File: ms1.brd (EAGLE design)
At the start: 160 x 100 mm, 146 parts, among them IC1 MAX3232EUE, IC2 MAX3380EEUP, J1 POWERPOLE_POWER25A, J10 Radio, J11 A3, J12 A4, J13 A5, J14 A6, J15 A7, J16 D1, J17 D2, J18 D3, J19 D4, J2 ON, J20 D5, J21 D6, J22 D7, J3 LED-EN, J4 RS232, J5 RS485, J6 A1, J7 I2C, J8 A2, J9 TTL_SERIAL, Q1 DMG6602SVT, Q2 DMG6602SVT, Q3 DMG6602SVT, Q4 DMG6602SVT, U1 LT1934ES6TRMPBF, U2 LT1934ES6TRMPBF, U3 DS3231SN, U4 ISL3179EIBZ, X1 KUSBVX-BS1N

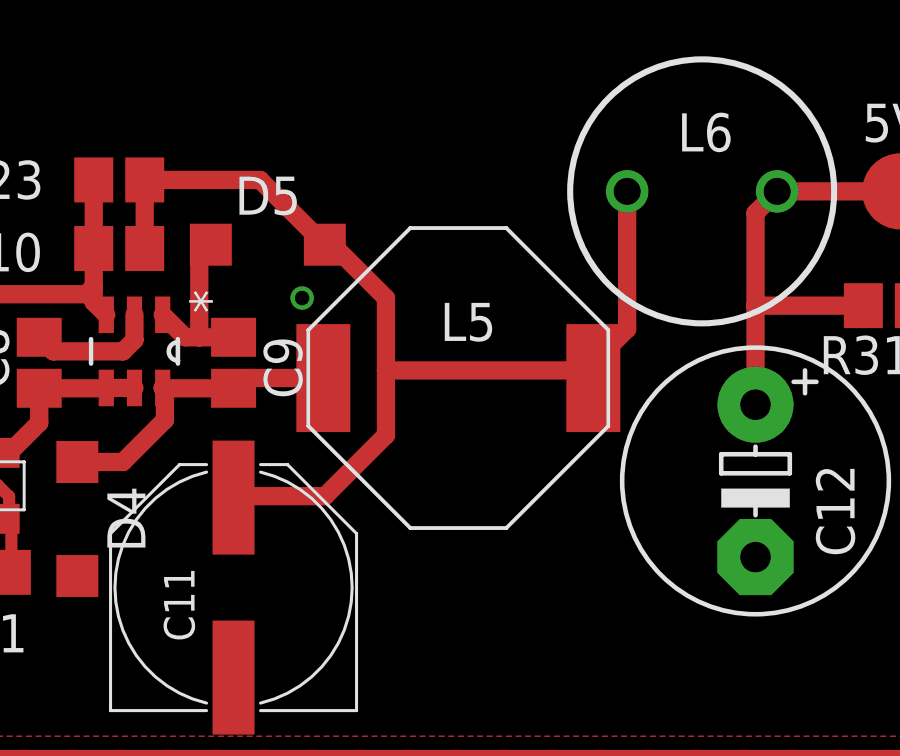
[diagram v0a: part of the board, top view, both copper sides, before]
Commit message: now uses dr127 for 5w inductor
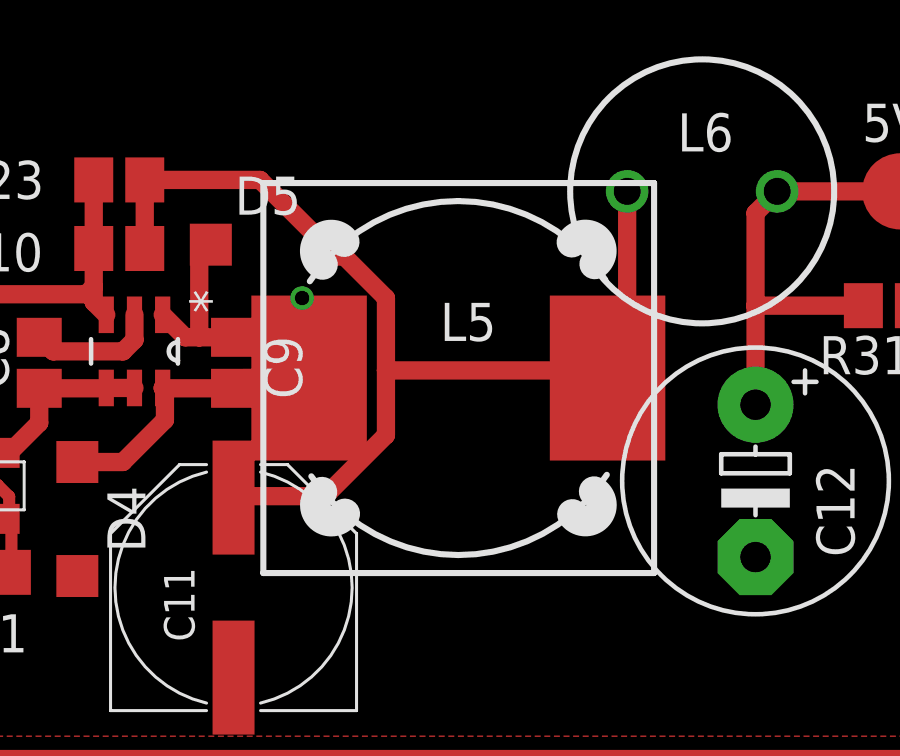
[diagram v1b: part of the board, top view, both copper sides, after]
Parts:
- L5: device farnell-parts:1048 -> inductors:DR127
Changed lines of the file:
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@@
 <attribute name="NAME" x="121.285" y="92.202" size="1.27" layer="25" rot="R180"/>
 </element>
-<element name="L5" library="farnell-parts" package="1048" value="68uH" x="135.128" y="87.376" smashed="yes">
+<element name="L5" library="inductors" package="DR127" value="68uH" x="135.128" y="87.376" smashed="yes">
 <attribute name="NAME" x="134.522" y="88.612" size="1.27" layer="25" ratio="10"/>
 </element>
@@
 <wire x1="125.2846" y1="87.034" x2="127.635" y2="87.034" width="0.6096" layer="1"/>
 <wire x1="127.635" y1="87.034" x2="127.977" y2="87.376" width="0.6096" layer="1"/>
-<wire x1="127.977" y1="87.376" x2="130.628" y2="87.376" width="0.6096" layer="1"/>
+<wire x1="127.977" y1="87.376" x2="130.153" y2="87.376" width="0.6096" layer="1"/>
 <wire x1="125.2728" y1="87.0458" x2="125.349" y2="86.9696" width="0.6096" layer="1"/>
 <wire x1="125.349" y1="86.9696" x2="125.349" y2="85.979" width="0.6096" layer="1"/>
@@
 <wire x1="132.715" y1="90.043" x2="130.937" y2="91.821" width="0.6096" layer="1"/>
 <wire x1="130.937" y1="91.821" x2="130.678" y2="91.821" width="0.6096" layer="1"/>
-<wire x1="139.628" y1="87.376" x2="139.374" y2="87.63" width="0.6096" layer="1"/>
+<wire x1="140.103" y1="87.376" x2="139.374" y2="87.63" width="0.6096" layer="1"/>
 <wire x1="139.374" y1="87.63" x2="132.715" y2="87.63" width="0.6096" layer="1"/>
 <wire x1="139.374" y1="87.63" x2="140.756" y2="89.012" width="0.6096" layer="1"/>

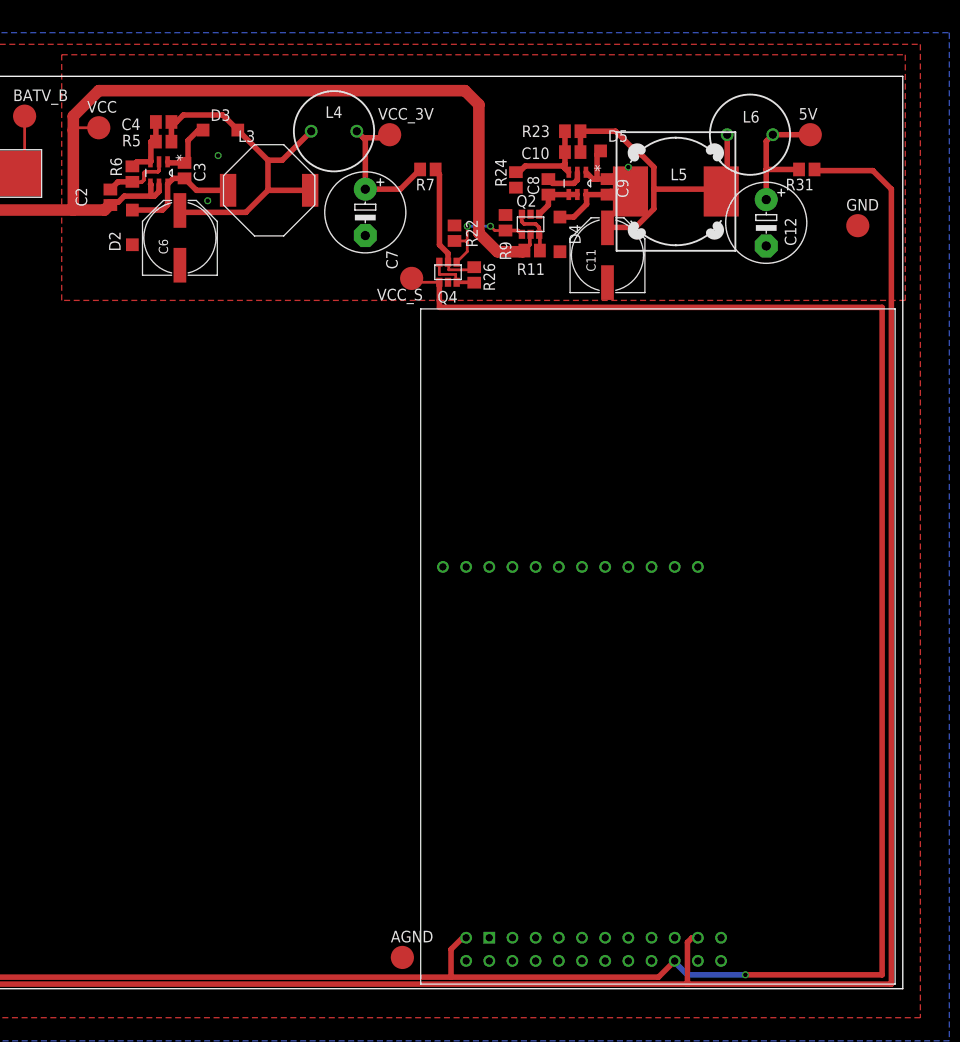
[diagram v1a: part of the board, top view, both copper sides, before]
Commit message: more smoothing to 5v rail
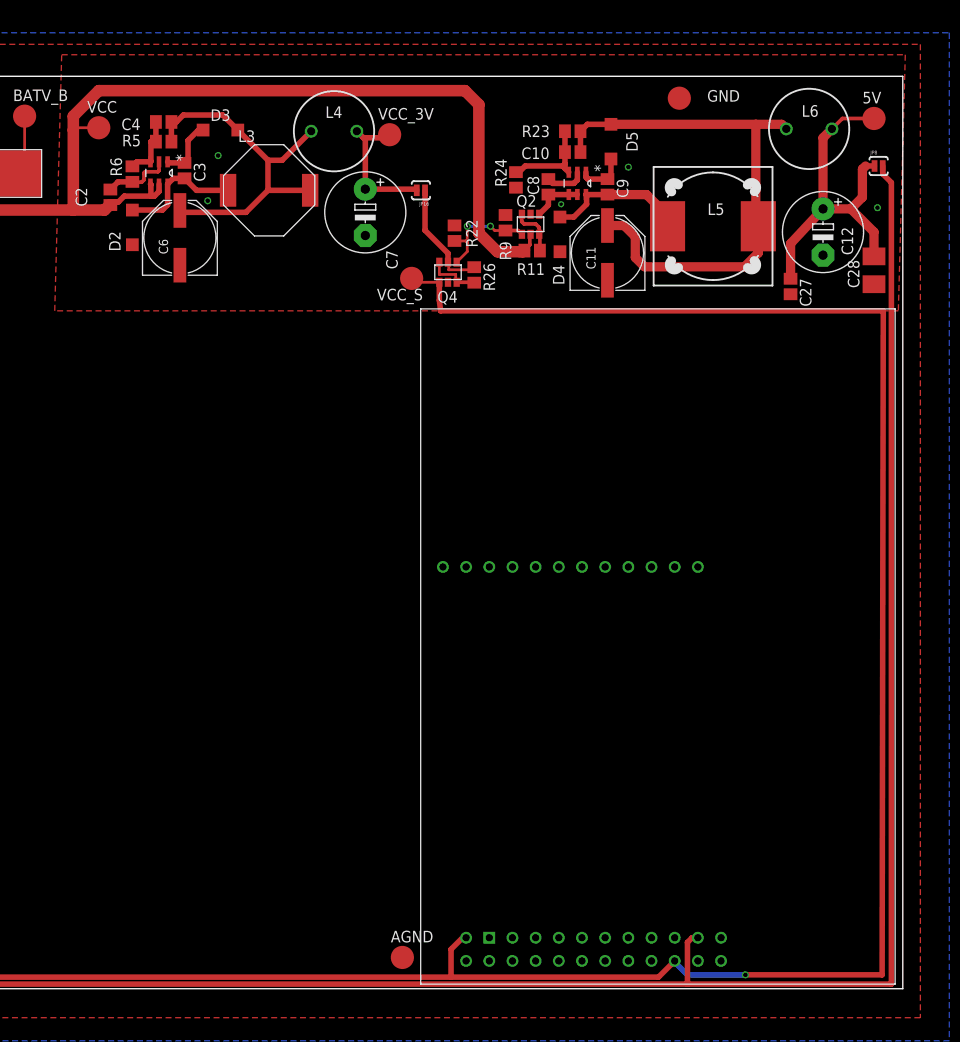
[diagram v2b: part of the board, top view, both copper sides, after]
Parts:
- removed R31, R7: TEST, resistor:R0805
- added C27: (no value), resistor:C0805
- added C28: (no value), resistor:B/3528-21R
- added JP16, JP8: (no value), SparkFun-Passives:SJ_2S-NO
- moved GND 24.0 mm to (135.5, 97.6)
- moved 5V 7.21 mm to (156.8, 95.4)
- moved L6 6.51 mm to (149.7, 94.2)
- moved C12 6.31 mm to (151.3, 82.9)
- moved L5 5.57 mm to (139.2, 83.6)
- moved D5 1.27 mm to (128.0, 92.8), turned to 90 degrees
- moved C11 0.25 mm to (127.6, 80.6)
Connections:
- net GND: now also C27.2, C28.-
- net N$13: now also JP16.2; no longer R7.2
- net N$14: now also C27.1, C28.+, JP8.1; no longer R31.2
- net SENSE_5V: now also JP8.2; no longer R31.1
- net VCC_3V3: now also JP16.1; no longer R7.1
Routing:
- net N$14: track 15.1 -> 39.0 mm
- net N$6: track 36.4 -> 60.1 mm
- net SENSE_5V: track 275.8 -> 269.4 mm
- net N$3: track 9.63 -> 15.7 mm
- net VCC_3V3: track 52.3 -> 50.6 mm
- net N$13: track 16.7 -> 15.5 mm
- net N$4: track 5.92 -> 5.35 mm
- net GND: vias 7 -> 9

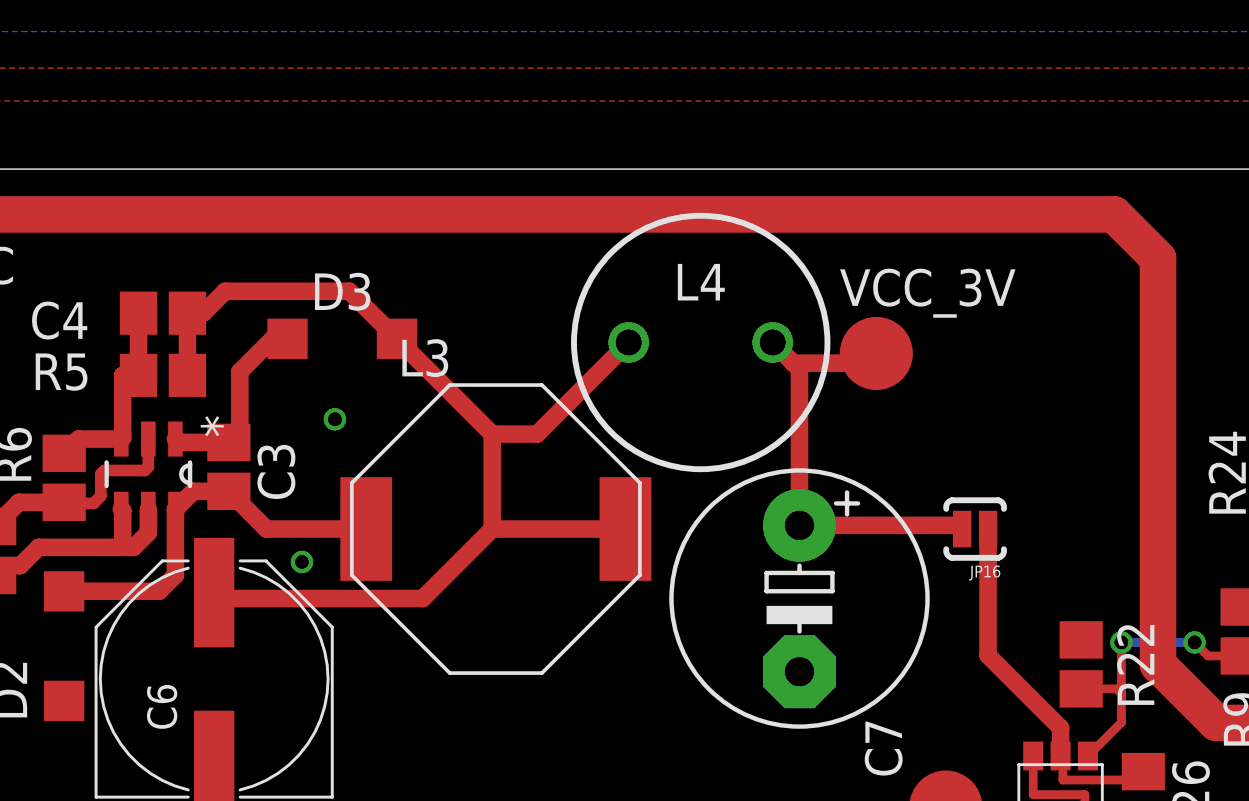
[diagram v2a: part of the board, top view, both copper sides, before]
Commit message: more smoothing on 3v3 output
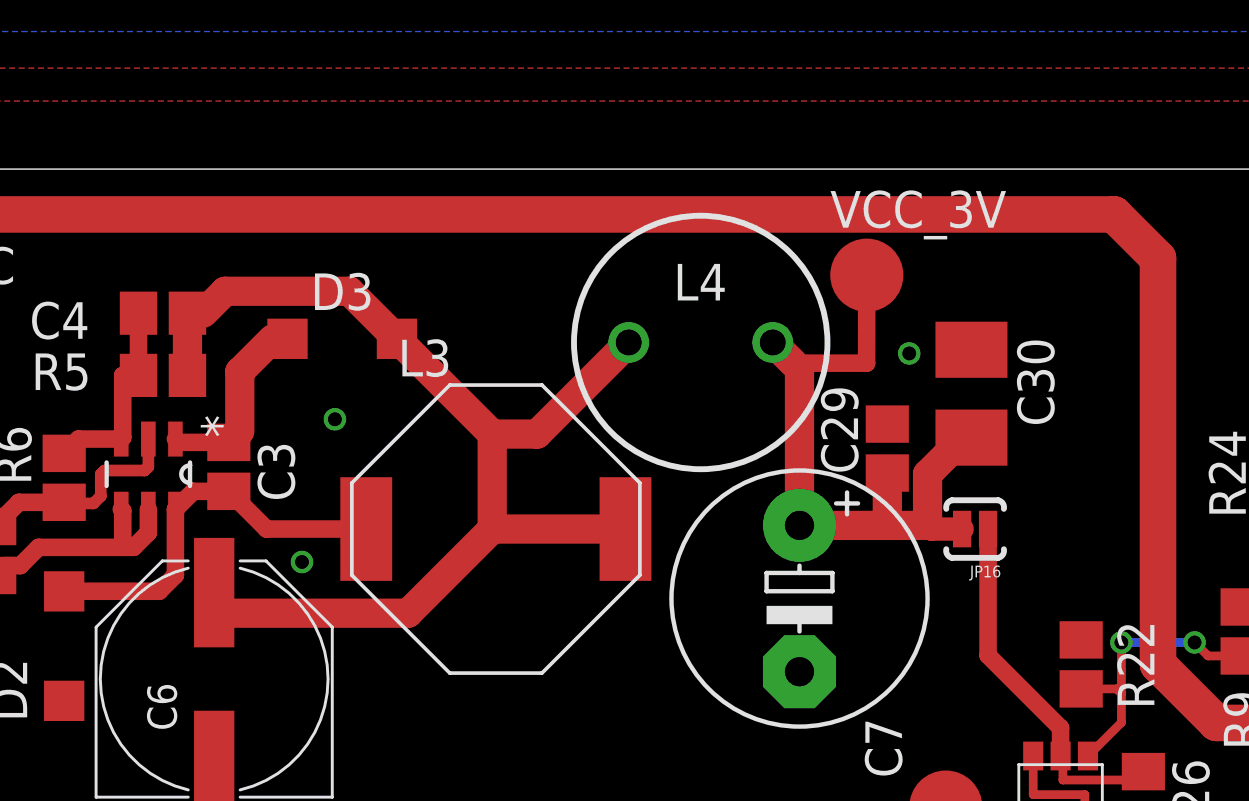
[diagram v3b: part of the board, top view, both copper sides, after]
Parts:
- added C29: (no value), resistor:C0805
- added C30: (no value), resistor:B/3528-21R
- moved VCC_3V 2.74 mm to (103.4, 96.3)
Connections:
- net GND: now also C29.2, C30.-
- net N$13: now also C29.1, C30.+
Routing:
- net N$13: track 15.5 -> 23.7 mm
- net N$107: track 39.8 -> 40.7 mm
- net GND: vias 9 -> 10
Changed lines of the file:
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@@
 <attribute name="NAME" x="84.117" y="95.107" size="1.27" layer="25"/>
 </element>
-<element name="VCC_3V" library="testpad" package="B2,54" value="TPB2,54" x="103.759" y="93.599">
-<attribute name="TP_SIGNAL_NAME" value="" x="210.439" y="-70.231" size="1.778" layer="27" display="off"/>
+<element name="VCC_3V" library="testpad" package="B2,54" value="TPB2,54" x="103.4288" y="96.3168">
+<attribute name="TP_SIGNAL_NAME" value="" x="210.1088" y="-67.5132" size="1.778" layer="27" display="off"/>
 </element>
 <element name="J2" library="farnell-parts" package="2-MOLEX" value="ON" x="5.715" y="96.2025" smashed="yes" rot="R270">
@@
 <element name="JP8" library="SparkFun-Passives" package="SJ_2S-NO" value="" x="157.353" y="90.17"/>
 <element name="JP16" library="SparkFun-Passives" package="SJ_2S-NO" value="" x="107.188" y="87.503" rot="R180"/>
+<element name="C29" library="resistor" package="C0805" value="" x="104.14" y="90.297" rot="R90"/>
+<element name="C30" library="resistor" package="B/3528-21R" value="" x="107.061" y="92.202" rot="R270"/>
 </elements>
 <signals>
@@
 <via x="122.555" y="85.979" extent="1-16" drill="0.381" shape="square"/>
 <via x="157.226" y="85.598" extent="1-16" drill="0.4826" shape="square"/>
+<contactref element="C30" pad="-"/>
+<contactref element="C29" pad="2"/>
+<via x="104.902" y="93.599" extent="1-16" drill="0.4826" shape="square"/>
 <wire x1="93.726" y1="136.017" x2="90.297" y2="143.549" width="0" layer="19" extent="16-16"/>
 <wire x1="93.726" y1="134.747" x2="93.726" y2="136.017" width="0" layer="19" extent="16-16"/>
@@
 <wire x1="84.328" y1="133.477" x2="84.328" y2="134.747" width="0" layer="19" extent="16-16"/>
 <wire x1="84.328" y1="132.207" x2="84.328" y2="133.477" width="0" layer="19" extent="16-16"/>
-<wire x1="84.963" y1="91.313" x2="93.726" y2="130.937" width="0" layer="19" extent="16-16"/>
+<wire x1="104.902" y1="93.599" x2="93.726" y2="130.937" width="0" layer="19" extent="16-16"/>
 <wire x1="-85.979" y1="97.663" x2="2.794" y2="64.516" width="0" layer="19" extent="1-1"/>
 <wire x1="-93.599" y1="97.663" x2="-85.979" y2="97.663" width="0" layer="19" extent="1-1"/>
@@
 <wire x1="79.541" y1="90.512" x2="81.28" y2="90.512" width="0.6096" layer="1"/>
 <wire x1="81.28" y1="90.512" x2="81.661" y2="90.893" width="0.6096" layer="1"/>
-<wire x1="81.661" y1="90.893" x2="81.661" y2="92.964" width="0.6096" layer="1"/>
-<wire x1="81.661" y1="92.964" x2="82.804" y2="94.107" width="0.6096" layer="1"/>
+<wire x1="81.661" y1="90.893" x2="81.661" y2="92.964" width="1.016" layer="1"/>
+<wire x1="81.661" y1="92.964" x2="82.804" y2="94.107" width="1.016" layer="1"/>
 <wire x1="82.804" y1="94.107" x2="83.317" y2="94.107" width="0.6096" layer="1"/>
 </signal>
@@
 <contactref element="C4" pad="1"/>
 <contactref element="L4" pad="1"/>
-<wire x1="79.844" y1="94.996" x2="79.844" y2="92.837" width="0.6096" layer="1"/>
-<wire x1="87.117" y1="94.107" x2="85.466" y2="95.758" width="0.6096" layer="1"/>
-<wire x1="85.466" y1="95.758" x2="81.153" y2="95.758" width="0.6096" layer="1"/>
-<wire x1="81.153" y1="95.758" x2="80.391" y2="94.996" width="0.6096" layer="1"/>
+<wire x1="79.844" y1="94.996" x2="79.844" y2="92.837" width="1.016" layer="1"/>
+<wire x1="87.117" y1="94.107" x2="85.466" y2="95.758" width="1.016" layer="1"/>
+<wire x1="85.466" y1="95.758" x2="81.153" y2="95.758" width="1.016" layer="1"/>
+<wire x1="81.153" y1="95.758" x2="80.391" y2="94.996" width="1.016" layer="1"/>
 <wire x1="80.391" y1="94.996" x2="79.844" y2="94.996" width="0.6096" layer="1"/>
-<wire x1="80.772" y1="85.296" x2="80.978" y2="85.09" width="0.6096" layer="1"/>
-<wire x1="80.978" y1="85.09" x2="88.011" y2="85.09" width="0.6096" layer="1"/>
-<wire x1="88.011" y1="85.09" x2="90.424" y2="87.503" width="0.6096" layer="1"/>
-<wire x1="90.424" y1="87.503" x2="95.051" y2="87.503" width="0.6096" layer="1"/>
-<wire x1="87.117" y1="94.107" x2="90.424" y2="90.8" width="0.6096" layer="1"/>
-<wire x1="90.424" y1="90.8" x2="90.424" y2="87.503" width="0.6096" layer="1"/>
-<wire x1="95.163" y1="93.98" x2="91.983" y2="90.8" width="0.6096" layer="1"/>
-<wire x1="91.983" y1="90.8" x2="90.424" y2="90.8" width="0.6096" layer="1"/>
+<wire x1="80.772" y1="85.296" x2="80.724" y2="84.582" width="0.6096" layer="1"/>
+<wire x1="80.724" y1="84.582" x2="87.503" y2="84.582" width="1.016" layer="1"/>
+<wire x1="87.503" y1="84.582" x2="90.424" y2="87.503" width="1.016" layer="1"/>
+<wire x1="90.424" y1="87.503" x2="95.051" y2="87.503" width="1.016" layer="1"/>
+<wire x1="87.117" y1="94.107" x2="90.424" y2="90.8" width="1.016" layer="1"/>
+<wire x1="90.424" y1="90.8" x2="90.424" y2="87.503" width="1.016" layer="1"/>
+<wire x1="95.163" y1="93.98" x2="91.983" y2="90.8" width="1.016" layer="1"/>
+<wire x1="91.983" y1="90.8" x2="90.424" y2="90.8" width="1.016" layer="1"/>
 </signal>
 <signal name="N$2">
@@
 <contactref element="C7" pad="+"/>
 <contactref element="VCC_3V" pad="TP"/>
-<wire x1="100.163" y1="93.98" x2="100.8815" y2="93.2615" width="0.6096" layer="1"/>
+<wire x1="100.163" y1="93.98" x2="100.8815" y2="93.2615" width="1.016" layer="1"/>
 <wire x1="100.8815" y1="93.2615" x2="101.092" y2="93.051" width="0.6096" layer="1"/>
-<wire x1="101.092" y1="93.051" x2="101.092" y2="87.63" width="0.6096" layer="1"/>
-<wire x1="103.759" y1="93.599" x2="103.4215" y2="93.2615" width="0.6096" layer="1"/>
+<wire x1="101.092" y1="93.051" x2="101.092" y2="87.63" width="1.016" layer="1"/>
+<wire x1="103.4288" y1="96.3168" x2="103.4215" y2="93.2615" width="0.6096" layer="1"/>
 <wire x1="103.4215" y1="93.2615" x2="100.8815" y2="93.2615" width="0.6096" layer="1"/>
+<wire x1="101.092" y1="87.63" x2="104.14" y2="87.63" width="1.016" layer="1"/>
+<contactref element="C29" pad="1"/>
+<contactref element="C30" pad="+"/>
+<wire x1="104.14" y1="87.63" x2="105.537" y2="87.63" width="1.016" layer="1"/>
+<wire x1="104.14" y1="89.447" x2="104.14" y2="87.63" width="1.016" layer="1"/>
+<wire x1="107.061" y1="90.677" x2="106.806" y2="90.677" width="1.016" layer="1"/>
+<wire x1="106.806" y1="90.677" x2="105.537" y2="89.408" width="1.016" layer="1"/>
+<wire x1="105.537" y1="89.408" x2="105.537" y2="87.63" width="1.016" layer="1"/>
 <contactref element="JP16" pad="2"/>
-<wire x1="101.092" y1="87.63" x2="106.611" y2="87.63" width="0.6096" layer="1"/>
-<wire x1="106.611" y1="87.63" x2="106.738" y2="87.503" width="0.6096" layer="1"/>
+<wire x1="106.738" y1="87.503" x2="105.664" y2="87.503" width="0.8128" layer="1"/>
+<wire x1="105.664" y1="87.503" x2="105.537" y2="87.63" width="0.8128" layer="1"/>
 </signal>
 <signal name="VCC_HP2_SW1">
